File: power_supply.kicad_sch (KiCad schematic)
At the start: 55 parts, among them Q2 Q_FDC6561AN, Q3 Q_BC817-25, SW9 1825232-1, U1 INA219BIDR, U2 MIC2250-1YD5-TR, U3 MCP73871T-2CCI/ML, U5 AP9101CAK6-ABTRG1

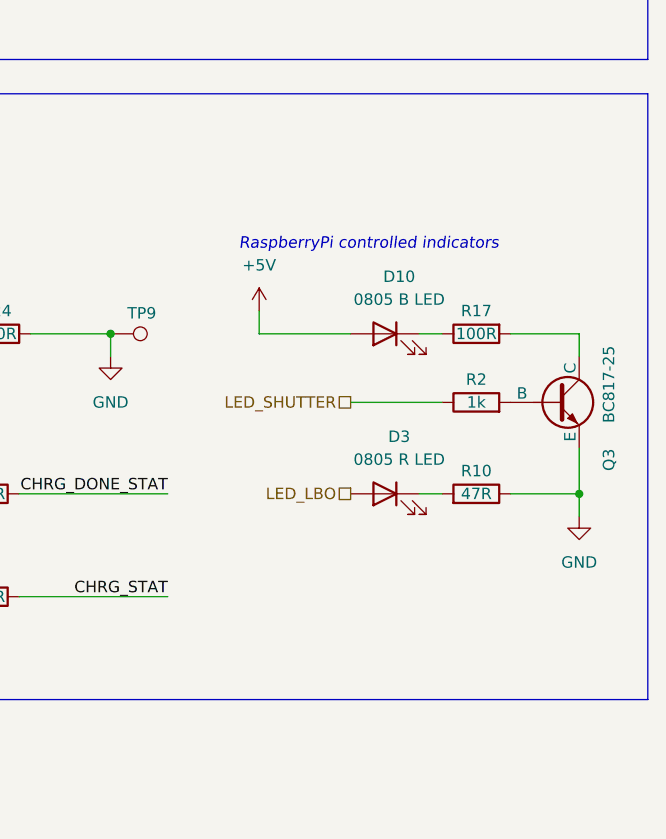
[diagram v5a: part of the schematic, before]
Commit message: Reroute USB, add shutter LED signal pulldown
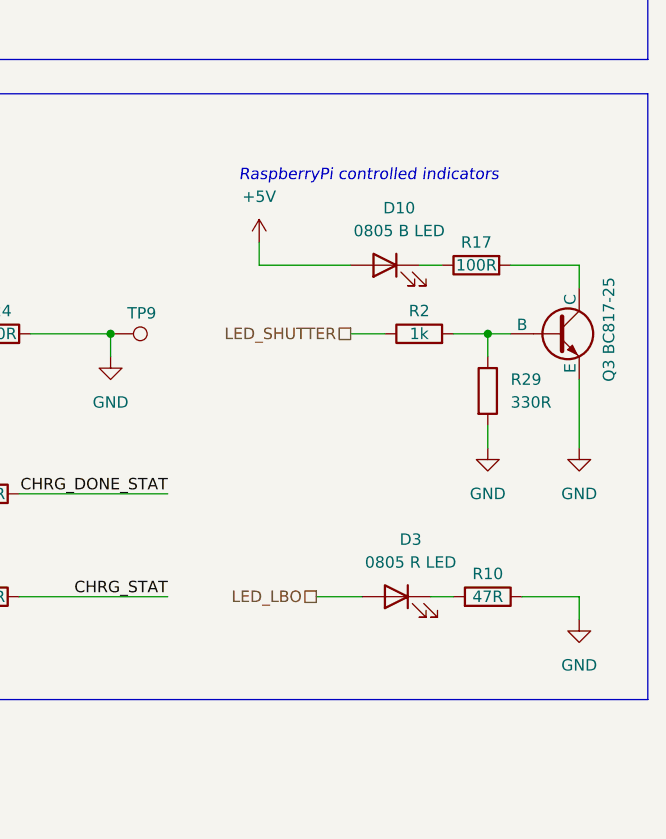
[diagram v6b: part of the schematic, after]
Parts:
- added R29: 330R, library:R_0402_1005Metric, symbol library:R_330R_0402
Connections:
- net GND: now also R29.2
- net at Q3.1 (B), R2.2: now also R29.1
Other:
- moved on the sheet: D10, D3, Q3, R10, R17, R2
